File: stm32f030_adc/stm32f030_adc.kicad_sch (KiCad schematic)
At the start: 19 parts, among them J1 SWD, J2 AudioJack3, U1 STM32F103C6Tx, U2 AMS1117-3.3, X1 USB_B_Micro

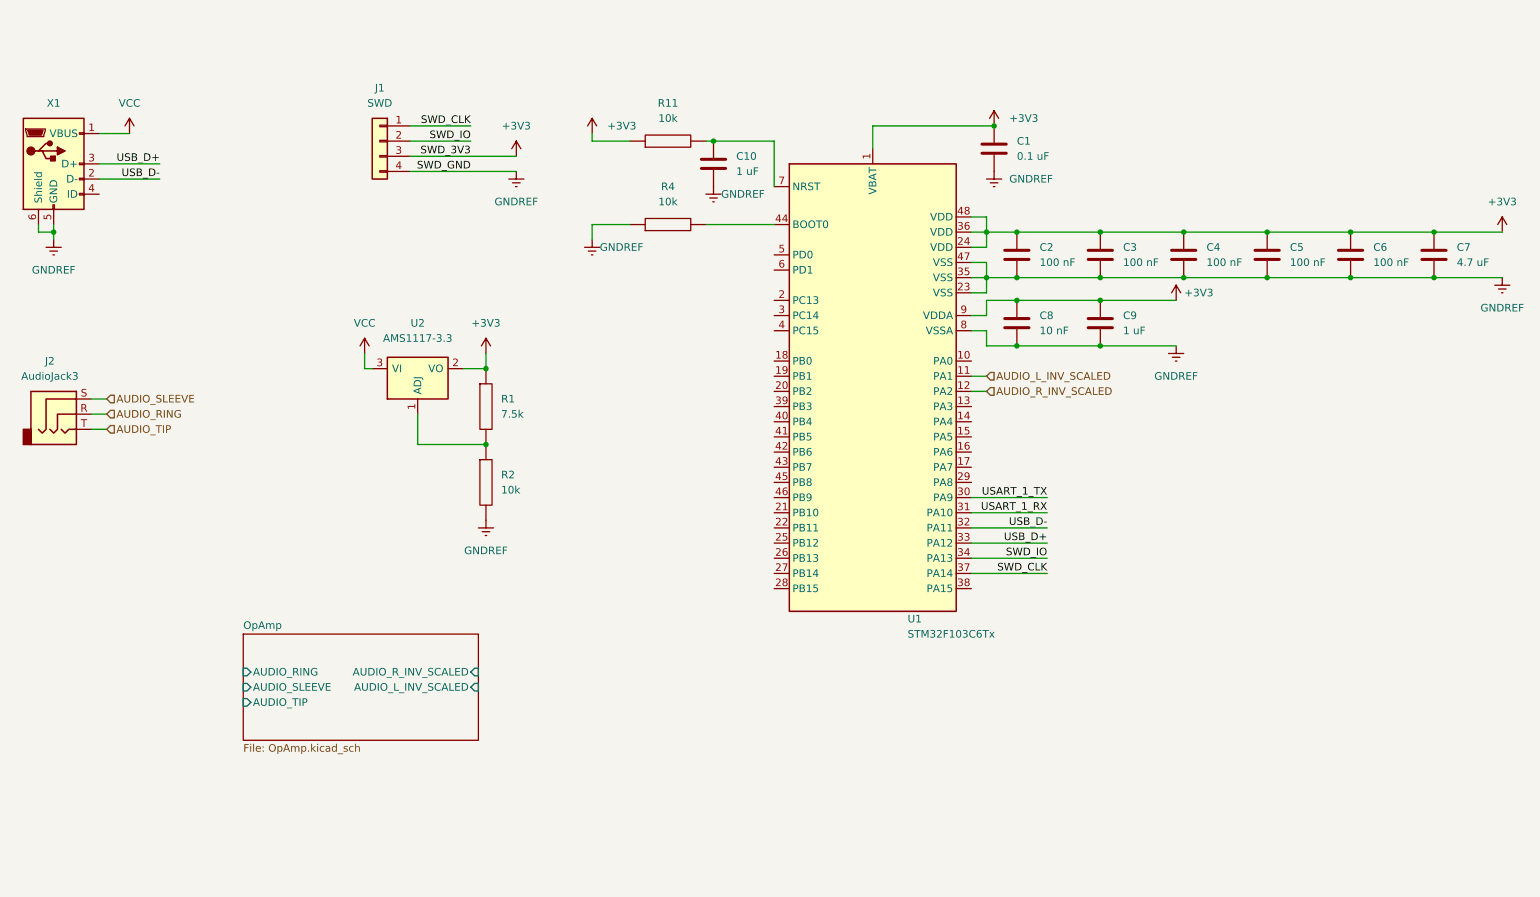
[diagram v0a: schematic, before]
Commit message: [stm32f030_adc] Bug | USB D+ pull-ups, filtering caps for AMS-1117, external 8MHz oscillator
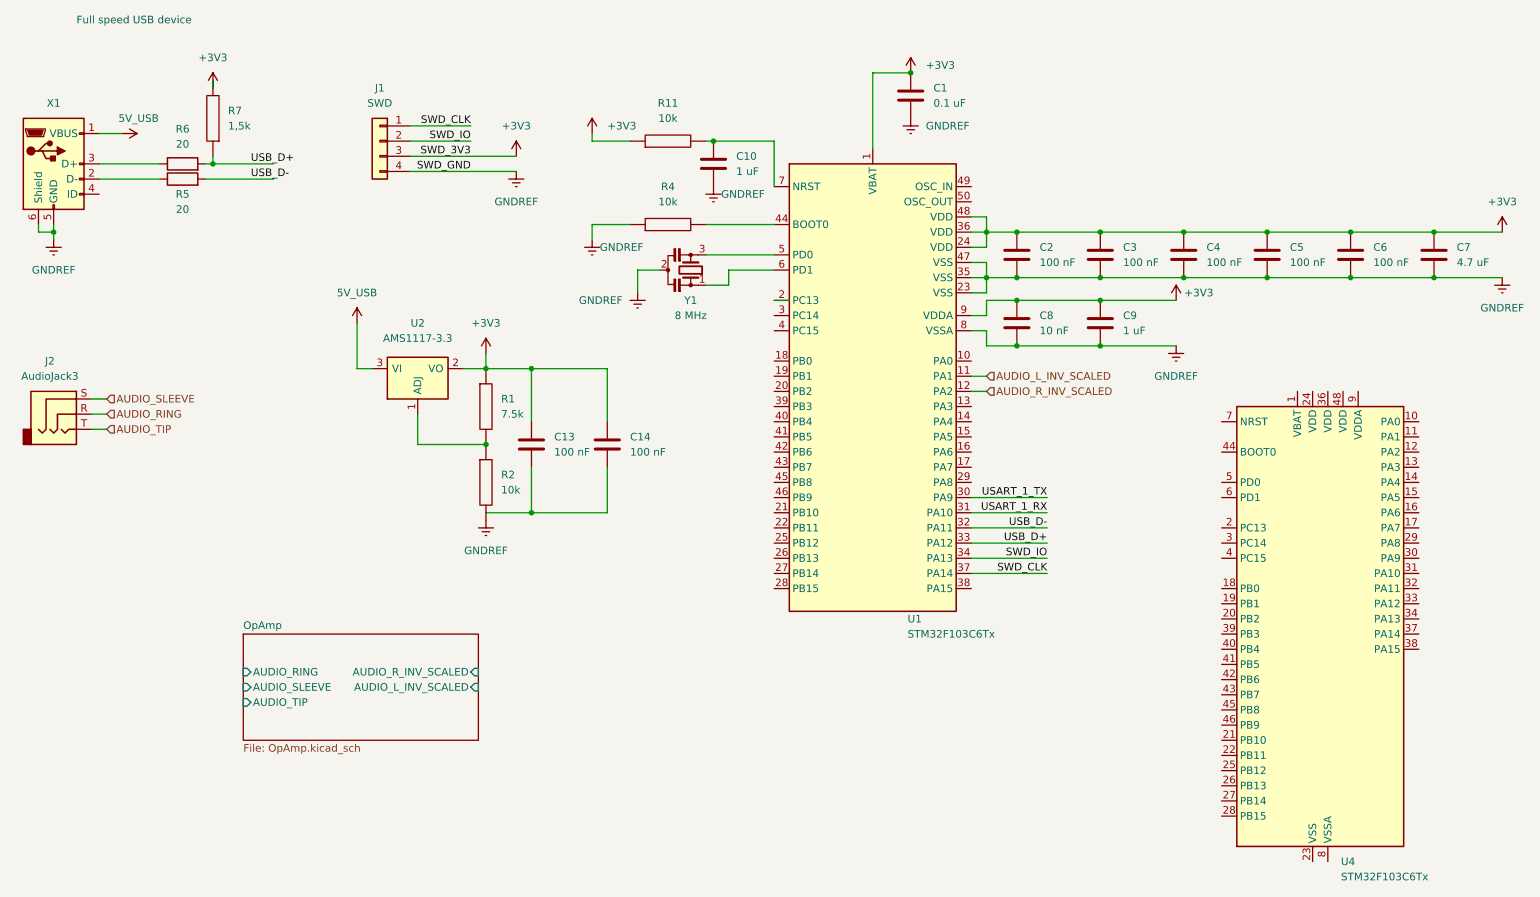
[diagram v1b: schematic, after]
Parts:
- added C13, C14: 100 nF, symbol Device:C
- added R5, R6: 20, symbol Device:R
- added R7: 1,5k, symbol pspice:R
- added U4: STM32F103C6Tx, Package_QFP:LQFP-48_7x7mm_P0.5mm, symbol MCU_ST_STM32F1:STM32F103C6Tx
- added Y1: 8 MHz, symbol Device:Resonator_Small
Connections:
- net +3V3: now also C13.1, C14.1, R7.2
- net GNDREF: now also Y1.2
- net USB_D+: now also R6.2, R7.1; no longer X1.3 (D+)
- net USB_D-: now also R5.2; no longer X1.2 (D-)
- net at U1.5 (PD0): now also Y1.3
- net at U1.6 (PD1): now also Y1.1
- net VCC renamed 5V_USB
- new net: U4.23 (VSS), U4.35 (VSS), U4.47 (VSS)
- new net: C13.2, C14.2
- new net: R6.1, X1.3 (D+)
- new net: R5.1, X1.2 (D-)
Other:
- note added: "Full speed USB device"
- moved on the sheet: C1

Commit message: [schematics] Impl | Replaced OpAmp w/ BJT-based amplifier (not biased yet), reorganized sheets: separated MCU from gain, added hierarchical connections
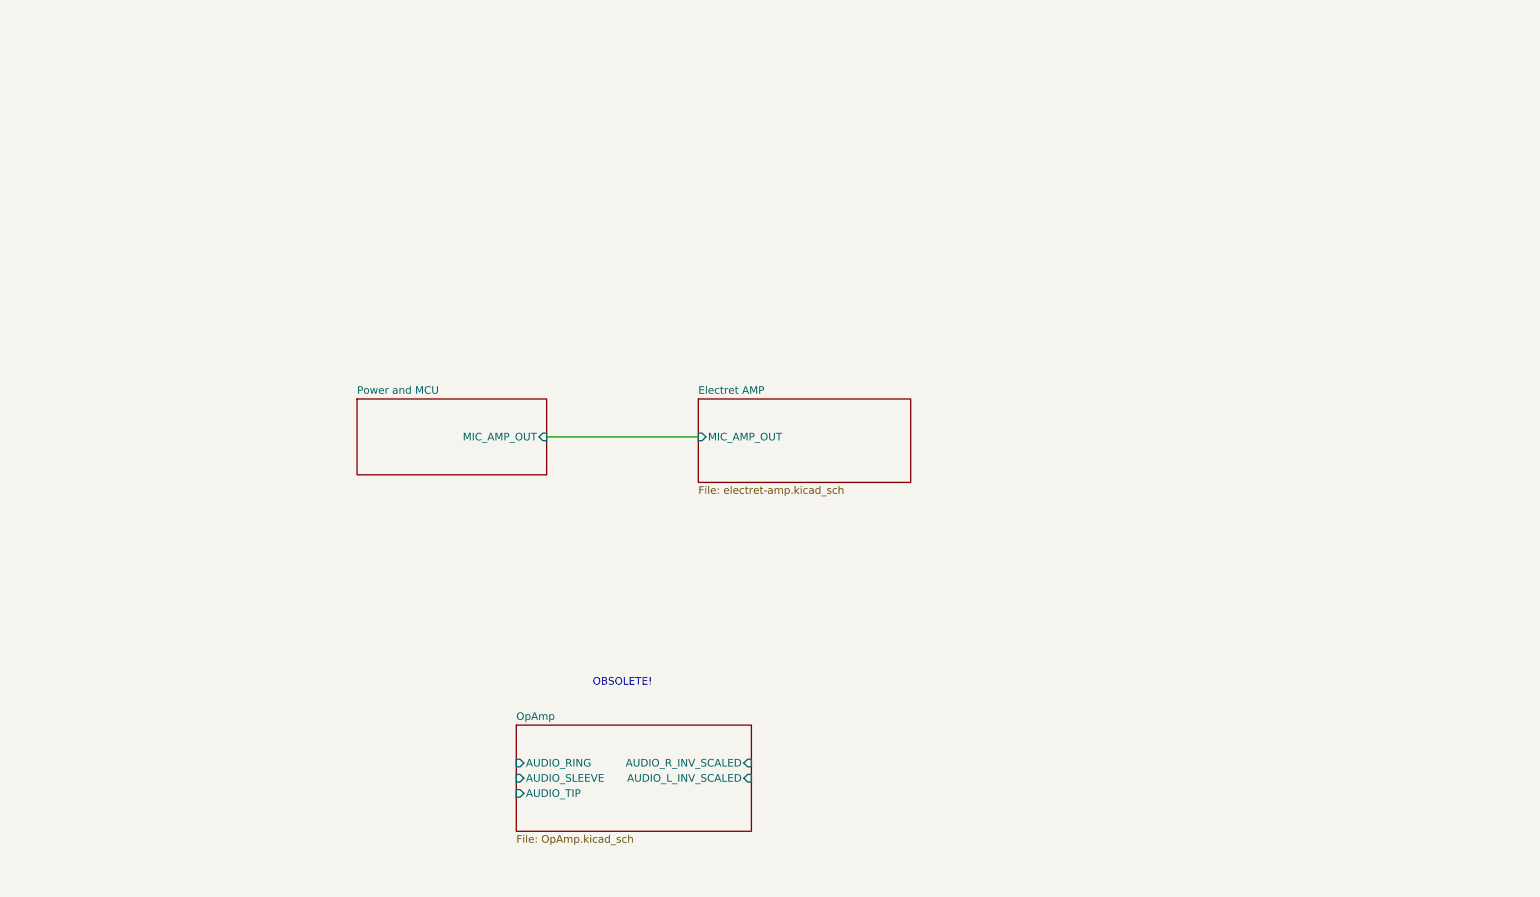
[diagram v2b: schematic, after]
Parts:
- removed C1: 0.1 uF, symbol Device:C
- removed C10, C9: 1 uF, symbol Device:C
- removed C13, C14, C2, C3, C4, C5, C6: 100 nF, symbol Device:C
- removed C7: 4.7 uF, symbol Device:C
- removed C8: 10 nF, symbol Device:C
- removed J1: SWD, symbol Connector_Generic:Conn_01x04
- removed J2: AudioJack3, symbol Connector:AudioJack3
- removed R1: 7.5k, symbol pspice:R
- removed R11, R2, R4: 10k, symbol pspice:R
- removed R5, R6: 20, symbol Device:R
- removed R7: 1,5k, symbol pspice:R
- removed U1, U4: STM32F103C6Tx, Package_QFP:LQFP-48_7x7mm_P0.5mm, symbol MCU_ST_STM32F1:STM32F103C6Tx
- removed U2: AMS1117-3.3, Package_TO_SOT_SMD:SOT-223-3_TabPin2, symbol Regulator_Linear:AMS1117
- removed X1: USB_B_Micro, symbol Connector:USB_B_Micro
- removed Y1: 8 MHz, symbol Device:Resonator_Small
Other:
- added sheet Electret AMP (electret-amp.kicad_sch)
- added sheet Power and MCU (power-mcu.kicad_sch)
- note added: "OBSOLETE!"
- note removed: "Full speed USB device"

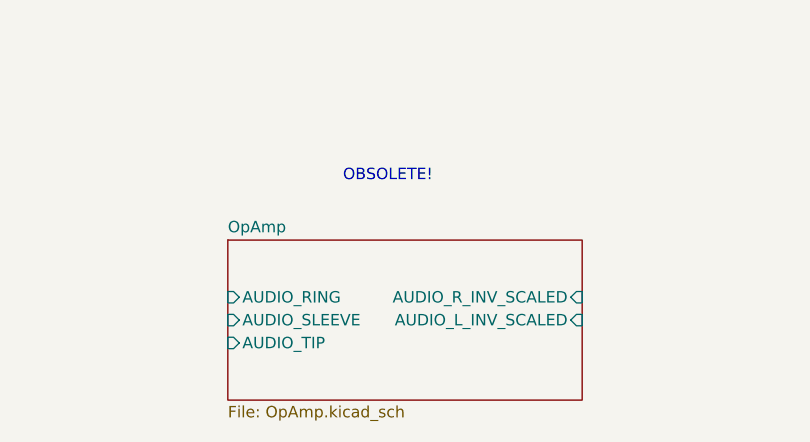
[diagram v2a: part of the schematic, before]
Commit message: Assigned footprints, removed obsolete parts
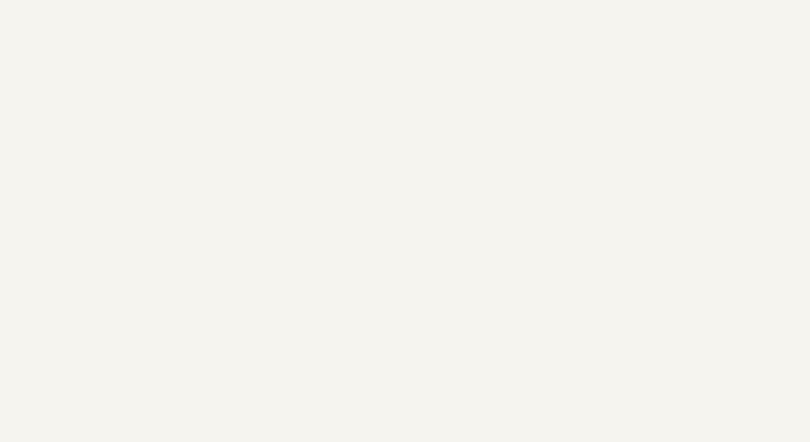
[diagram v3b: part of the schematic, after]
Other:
- removed sheet OpAmp
- note removed: "OBSOLETE!"
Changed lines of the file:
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@@
-		)
-	)
-	(text "OBSOLETE!\n"
-		(exclude_from_sim no)
-		(at 129.54 130.048 0)
-		(effects
-			(font
-				(size 1.27 1.27)
-			)
 		)
 	)
@@
 				)
 			)
-		)
-	)
-	(sheet
-		(at 111.76 137.16)
-		(size 39.37 17.78)
-		(fields_autoplaced yes)
-		(stroke
-			(width 0.1524)
-			(type solid)
-		)
-		(fill
-			(color 0 0 0 0.0000)
-		)
-		(property "Sheetname" "OpAmp"
-			(at 111.76 136.4484 0)
-			(effects
-				(font
-					(size 1.27 1.27)
-				)
-				(justify left bottom)
-			)
-		)
-		(property "Sheetfile" "OpAmp.kicad_sch"
-			(at 111.76 155.5246 0)
-			(effects
-				(font
-					(size 1.27 1.27)
-				)
-				(justify left top)
-			)
-		)
-		(pin "AUDIO_RING" input
-			(at 111.76 143.51 180)
-			(effects
-				(font
-					(size 1.27 1.27)
-				)
-				(justify left)
-			)
-		)
-		(pin "AUDIO_SLEEVE" input
-			(at 111.76 146.05 180)
-			(effects
-				(font
-					(size 1.27 1.27)
-				)
-				(justify left)
-			)
-		)
-		(pin "AUDIO_R_INV_SCALED" input
-			(at 151.13 143.51 0)
-			(effects
-				(font
-					(size 1.27 1.27)
-				)
-				(justify right)
-			)
-		)
-		(pin "AUDIO_TIP" input
-			(at 111.76 148.59 180)
-			(effects
-				(font
-					(size 1.27 1.27)
-				)
-				(justify left)
-			)
-		)
-		(pin "AUDIO_L_INV_SCALED" input
-			(at 151.13 146.05 0)
-			(effects
-				(font
-					(size 1.27 1.27)
-				)
-				(justify right)
-			)
-		)
-		(instances
-			(project "stm32f030_adc"
-				(path "/85629656-c73b-4e1f-b8e8-4366f4b01266"
-					(page "2")
-				)
-			)
